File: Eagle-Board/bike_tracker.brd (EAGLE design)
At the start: 100 x 80 mm, 16 parts, among them J1 TRANSFLASH-LOCK

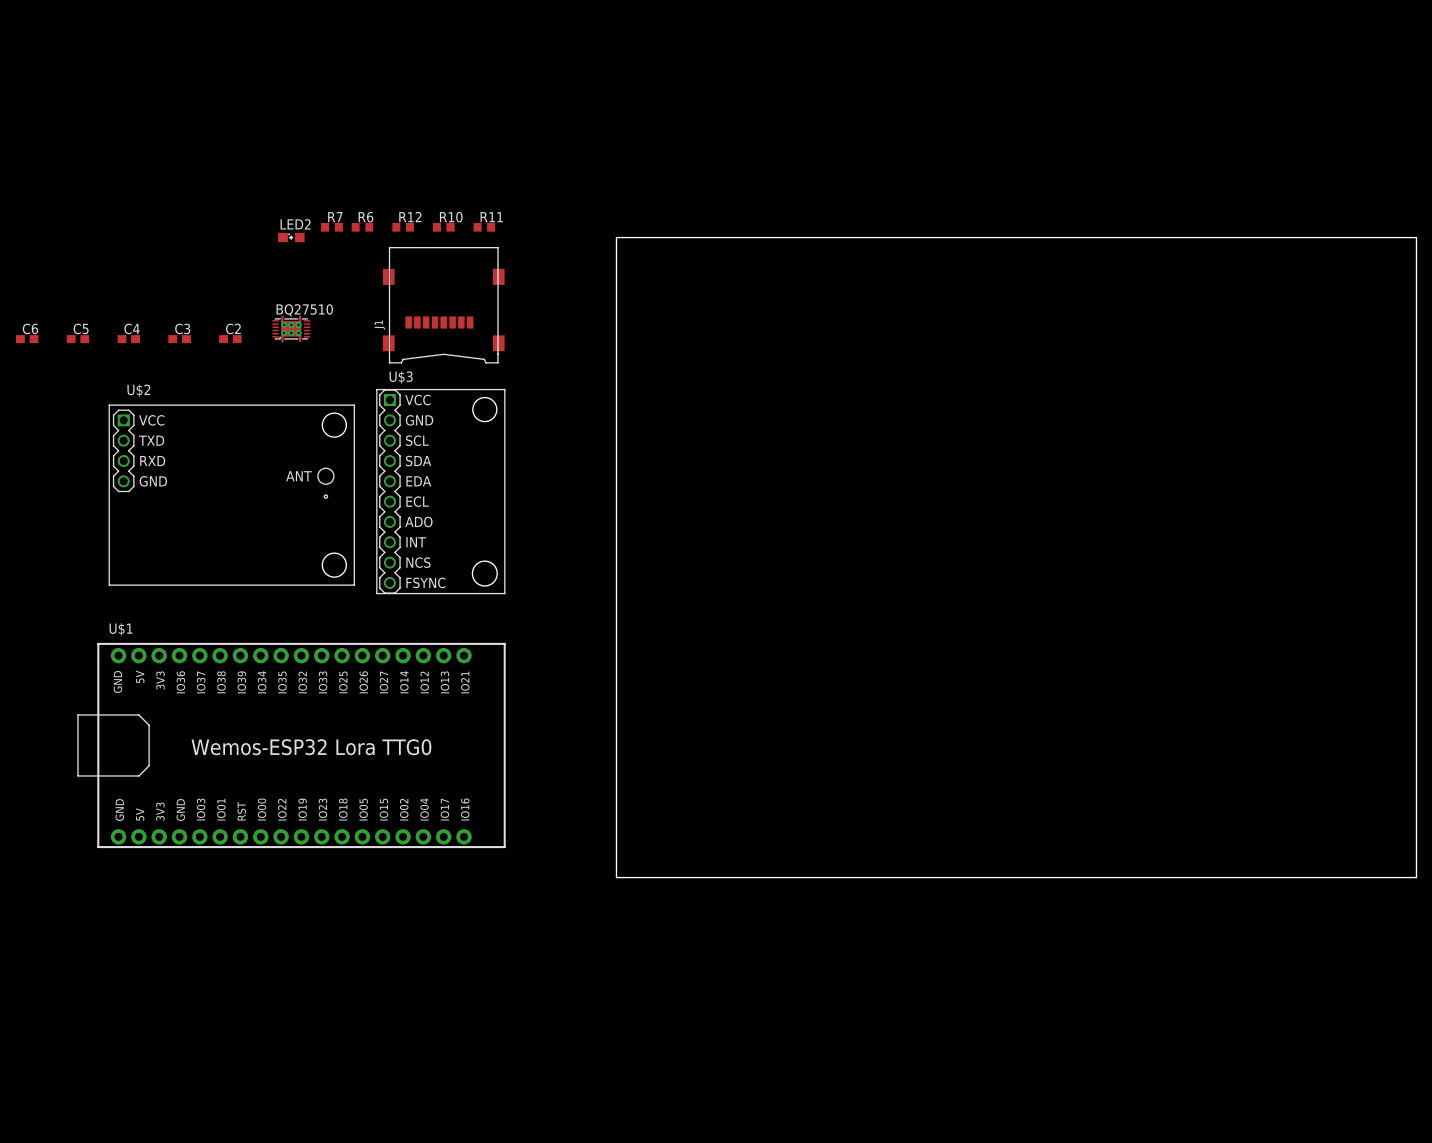
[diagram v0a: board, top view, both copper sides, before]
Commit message: board design ready - revising and exporting for gerber - SeeedStudio Fusion files added
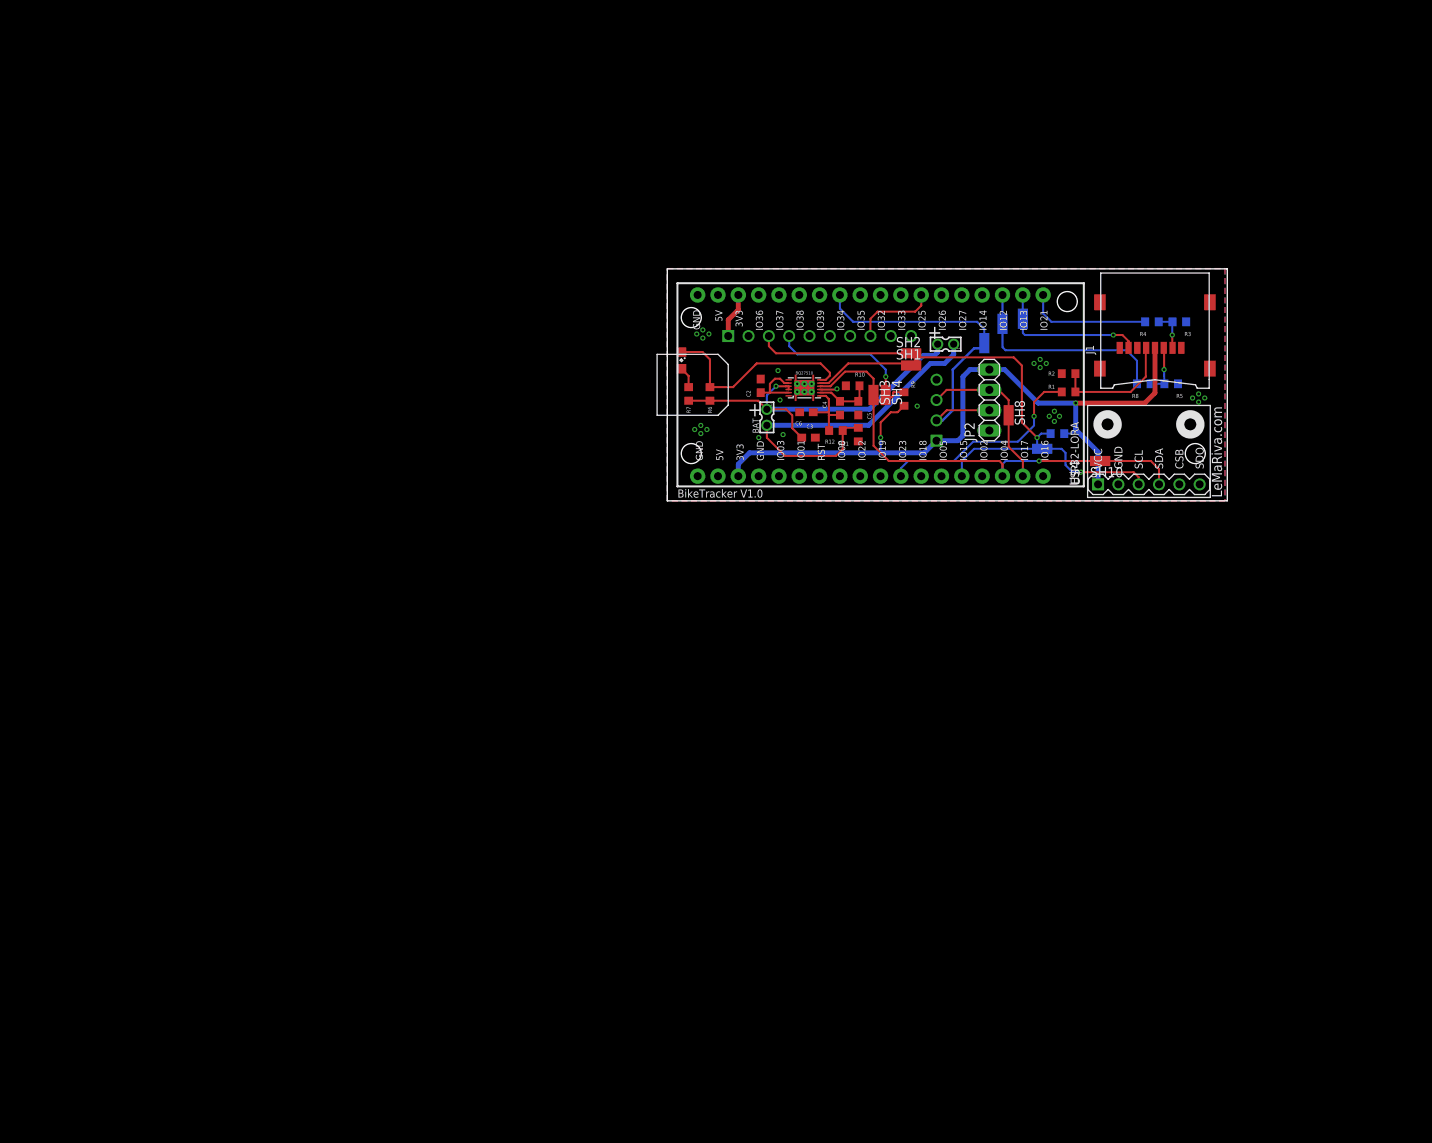
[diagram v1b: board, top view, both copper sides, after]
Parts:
- removed LED2: (no value), led:SML0805
- removed U$1: ESP32LORA, ESP32-DEVKITC:ESP32-LORA-TTGO
- added BAT, BAT-IN: 332-02, con-garry:332-02
- added ESP32-LORA: ESP32LORA, ESP32-DEVKITC:ESP32-LORA-TTGO
- added JP2: (no value), pinhead:1X04
- added LOW-BAT: (no value), led:SML0805
- added R1, R4, R8: 4k7, resistor:R0603
- added R13, R2, R3, R5, R9: 10k, resistor:R0603
- added SH1, SH10, SH2, SH3, SH4, SH5, SH6, SH7, SH8, SH9: SHORTT5, shorts:SHORT_TOP-50
- added U$4: BME280, diy-modules:BME280
- C4, C5, C6: value 0.47u -> 0.1u
- U$3: value IMU9255 -> MPU9255
- moved U$2 103.1 mm to (54.6, 64.8), flipped to the bottom, turned to 180 degrees
- moved C5 97.9 mm to (30.2, 58.7), turned to 270 degrees
- moved C6 97.8 mm to (23.7, 58.2)
- moved C4 89.3 mm to (27.9, 58.7), turned to 270 degrees
- moved J1 89.0 mm to (67.3, 66.7)
- moved C3 79.6 mm to (24.0, 55.0)
- moved C2 66.6 mm to (18.0, 61.5), turned to 90 degrees
- moved BQ27510 64.6 mm to (23.5, 61.2)
- moved R12 59.8 mm to (27.4, 55.9)
- moved R10 54.8 mm to (29.5, 61.5)
- moved R11 53.4 mm to (30.2, 55.4), turned to 90 degrees
- moved R7 49.2 mm to (9.02, 60.5), turned to 270 degrees
- moved R6 48.2 mm to (11.7, 60.5), turned to 270 degrees
- moved U$3 45.6 mm to (24.1, 59.7), flipped to the bottom, turned to 270 degrees
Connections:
- removed net RXD: U$2.3
- removed net VCC: U$3.1
- new net INT-IMU: ESP32-LORA.25, U$3.8
- new net MISO-SD: J1.7, SH6.1
- new net MOSI-SD: R8.2, SH5.1
- new net N$1: J1.5, R1.1, R2.2
- new net N$2: J1.2, R3.2, R4.1
- new net N$3: J1.3, R5.2, R8.1
- new net RX: ESP32-LORA.29, SH7.2
- new net RXD_NEO: JP2.3, SH8.1, U$2.3
- new net SCL: ESP32-LORA.14, R13.2, SH1.2, SH2.2, SH9.2
- new net SCL-BME: SH9.1, U$4.3
- new net SCL-IMU: SH2.1, U$3.3
- new net SDA: ESP32-LORA.16, R9.2, SH10.2, SH3.2, SH4.2
- new net SDA-BME: SH10.1, U$4.4
- new net SDA-IMU: SH4.1, U$3.4
- new net SPI-CLK: ESP32-LORA.11, R1.2
- new net SPI-CS: ESP32-LORA.19, R4.2
- new net SPI-MISO: ESP32-LORA.21, SH5.2
- new net SPI-MOSI: ESP32-LORA.20, SH6.2
- new net TX: ESP32-LORA.17, SH8.2
- new net TXD-NEO: JP2.2, SH7.1, U$2.2
- net !BAT_LOW: now also LOW-BAT.C; no longer LED2.C
- net 5V: now also ESP32-LORA.2, ESP32-LORA.35; no longer U$1.2, U$1.35
- net GND: now also ESP32-LORA.1, ESP32-LORA.36, ESP32-LORA.4, JP2.1, R2.1, R3.1, R5.1, U$2.4, U$4.2; no longer U$1.1, U$1.36, U$1.4
- net N$9: now also LOW-BAT.A; no longer LED2.A
- net SCL_BQ27510: now also SH1.1
- net SDA_BQ27510: now also SH3.1
- net VBAT+: now also BAT-IN.2, BAT.1
- net VBAT-: now also BAT-IN.1, BAT.2
- net VDD: now also ESP32-LORA.3, ESP32-LORA.34, JP2.4, R13.1, R9.1, U$2.1, U$3.1, U$4.1
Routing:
- net VDD: track 0.00 -> 97.0 mm, vias 0 -> 2
- net VBAT+: track 0.00 -> 47.7 mm, vias 0 -> 1
- net VBAT-: track 0.00 -> 45.1 mm
- net SDA: track 0.00 -> 42.0 mm, vias 0 -> 1
- net SCL: track 0.00 -> 40.5 mm, vias 0 -> 1
- net SPI-CLK: track 0.00 -> 26.8 mm, vias 0 -> 1
- net !BAT_LOW: track 0.00 -> 25.9 mm
- net MOSI-SD: track 0.00 -> 22.7 mm
- net RX: track 0.00 -> 21.9 mm
- net TXD-NEO: track 0.00 -> 19.8 mm
- net SCL-IMU: track 0.00 -> 18.8 mm
- net SDA-IMU: track 0.00 -> 17.1 mm, vias 0 -> 1
- net MISO-SD: track 0.00 -> 15.6 mm, vias 0 -> 1
- net SPI-CS: track 0.00 -> 15.5 mm
- net N$1: track 0.00 -> 15.5 mm
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- added copper zone on layer 1, net GND
- added copper zone on layer 16, net GND
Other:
- board size 100 x 80 mm -> 70 x 29 mm
- board text added: "+"
- board text added: "BikeTracker V1.0"
- board text added: "LeMaRiva.com"

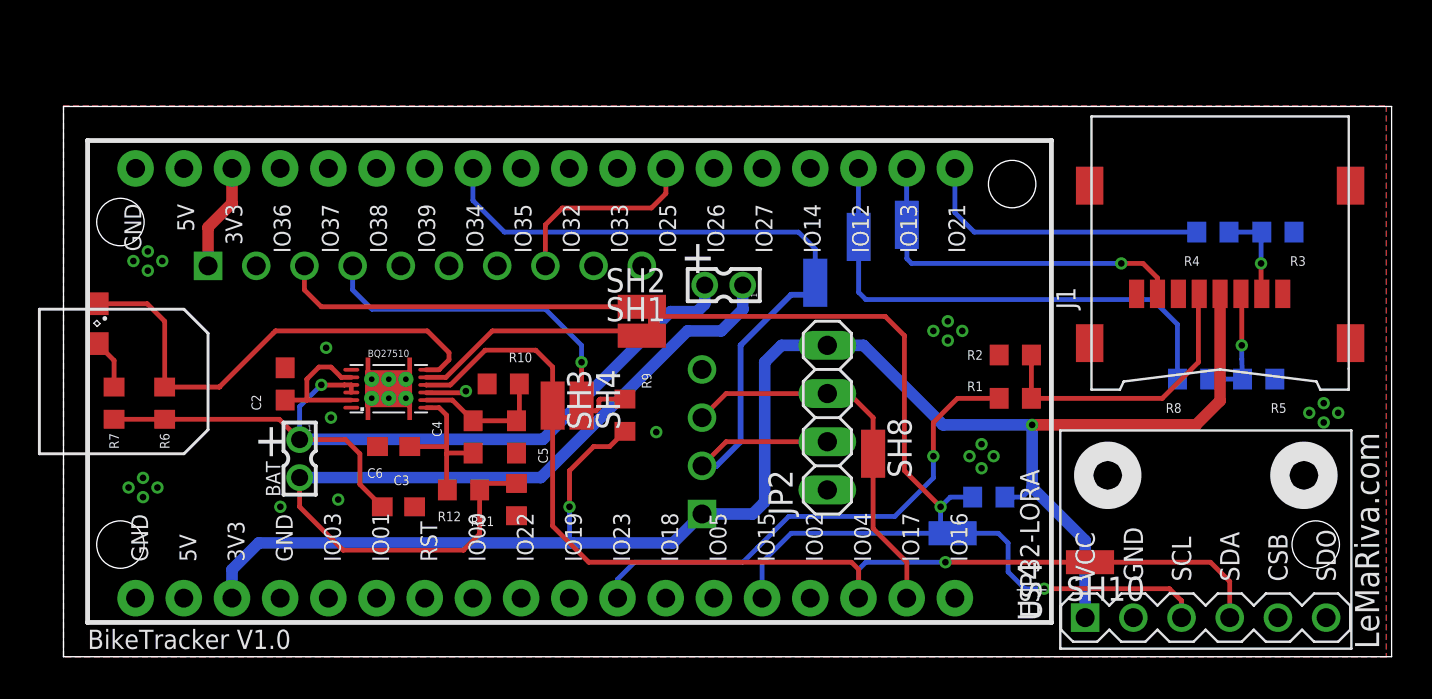
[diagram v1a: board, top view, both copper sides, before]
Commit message: texas and switch libraries added final version with buttons and possibility to switch off/on external devices
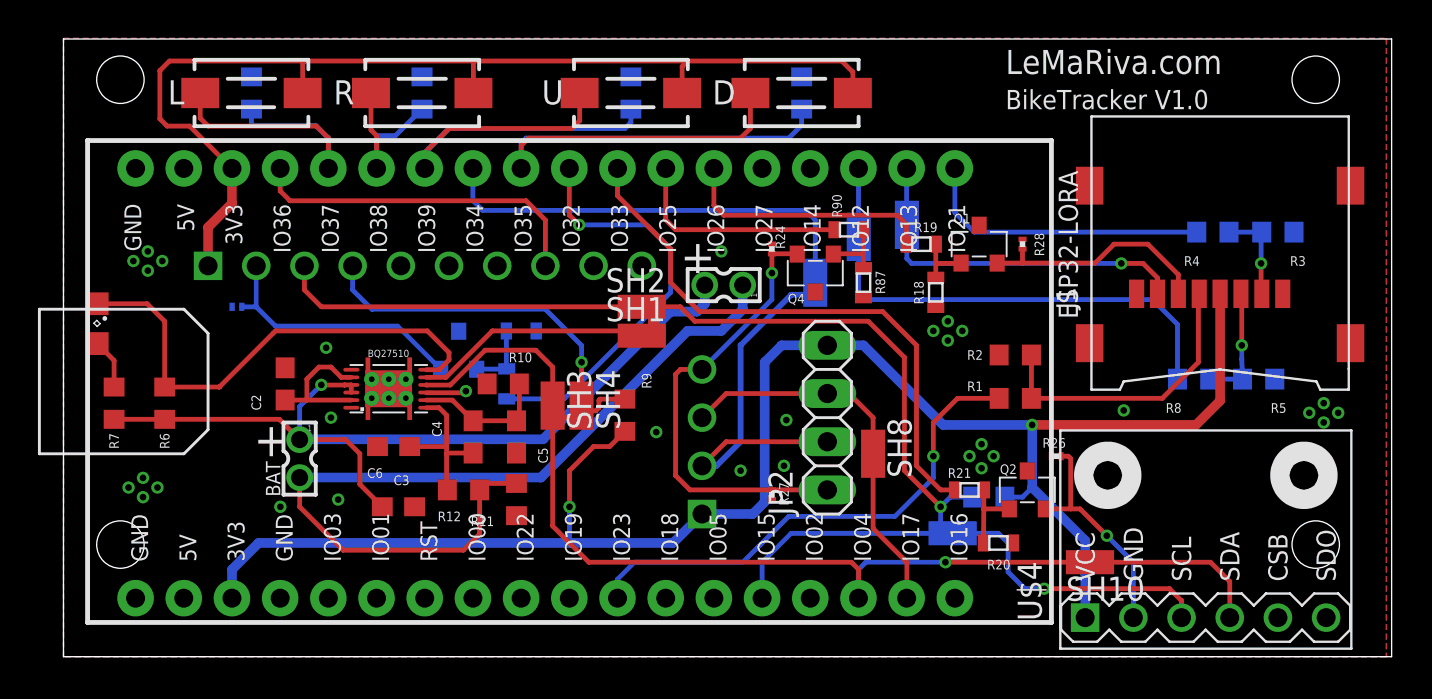
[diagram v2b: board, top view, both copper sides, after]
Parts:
- added D, L, R, U: DTSM-3, switch-tact:DTSM-3
- added Q1, Q2, Q3, Q4: IRLML5203, transistor-power:MICRO3
- added R14, R15, R16, R17: 10k, resistor:R0603
- added R18, R20, R22, R87: 10k, ssmd:0603
- added R19, R21, R23, R90: 470R, ssmd:0603
- added R24, R25, R26, R27, R28: (no value), resistor:R0201
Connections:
- new net GND_BME: Q2.2, R26.2, U$4.2
- new net GND_GPS: JP2.1, Q4.2, R24.2, R27.2, U$2.4
- new net GND_MPU: Q3.2, R25.2, U$3.2
- new net GND_SD: J1.6, Q1.2, R28.1
- new net IO25: ESP32-LORA.25, R90.2
- new net IO26: ESP32-LORA.24, R19.2
- new net IO32: ESP32-LORA.27, R23.2
- new net IO33: ESP32-LORA.26, R21.2
- new net IO35: D.1, ESP32-LORA.28, R17.2
- new net IO37: ESP32-LORA.32, L.1, R15.2
- new net IO38: ESP32-LORA.31, R.1, R16.2
- new net IO39: ESP32-LORA.30, R14.2, U.1
- new net N$12: ESP32-LORA.13
- new net N$4: Q4.1, R87.2, R90.1
- new net N$5: Q1.1, R18.2, R19.1
- new net N$6: Q2.1, R20.2, R21.1
- new net N$8: Q3.1, R22.2, R23.1
- net GND: now also Q1.3, Q2.3, Q3.3, Q4.3, R14.1, R15.1, R16.1, R17.1, R18.1, R20.1, R22.1, R24.1, R25.1, R26.1, R27.1, R28.2, R87.1; no longer J1.6, JP2.1, U$2.4, U$3.2, U$4.2
- net INT-IMU: now also ESP32-LORA.33; no longer ESP32-LORA.25
- net VDD: now also D.2, L.2, R.2, U.2
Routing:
- net VDD: track 97.0 -> 147.7 mm
- net IO35: track 0.00 -> 32.9 mm
- net IO33: track 0.00 -> 30.4 mm
- net IO39: track 0.00 -> 24.2 mm
- net GND_GPS: track 0.00 -> 24.1 mm, vias 0 -> 1
- net IO32: track 0.00 -> 21.8 mm, vias 0 -> 1
- net IO37: track 0.00 -> 16.8 mm
- net GND_MPU: track 0.00 -> 14.0 mm
- net IO26: track 0.00 -> 13.6 mm
- net GND_SD: track 0.00 -> 12.4 mm
- net GND_BME: track 0.00 -> 11.9 mm, vias 0 -> 1
- net IO25: track 0.00 -> 11.8 mm
- net IO38: track 0.00 -> 8.80 mm
- net INT-IMU: track 10.5 -> 18.2 mm
- net PWPD: track 0.00 -> 5.43 mm
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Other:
- board size 70 x 29 mm -> 70 x 32.6 mm

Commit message: minor modifications made
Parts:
- moved Q1 2.01 mm to (55.8, 67.2)
- moved R28 1.63 mm to (57.9, 67.6), turned to 180 degrees
- moved R26 1.28 mm to (57.4, 57.8)
- moved U$2 0.63 mm to (55.2, 64.8)
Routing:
- net TXD-NEO: track 19.8 -> 17.7 mm
- net N$5: track 3.11 -> 4.94 mm
- net GND_BME: track 11.9 -> 13.3 mm
- net GND_SD: track 12.4 -> 13.3 mm
- net RXD_NEO: track 11.3 -> 10.7 mm
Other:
- board size 70 x 32.6 mm -> 70 x 33 mm

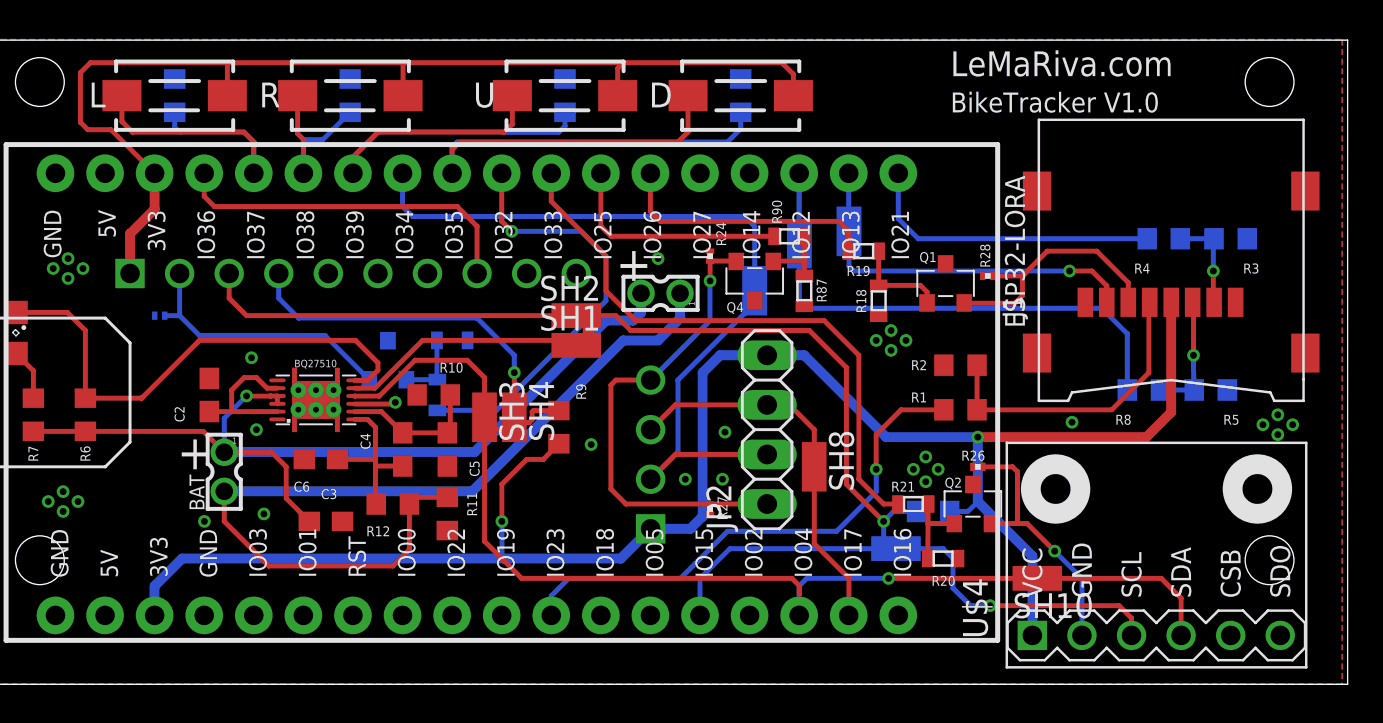
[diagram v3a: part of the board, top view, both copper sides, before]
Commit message: updated rev1.1 -> added RTC chip (DS1339)
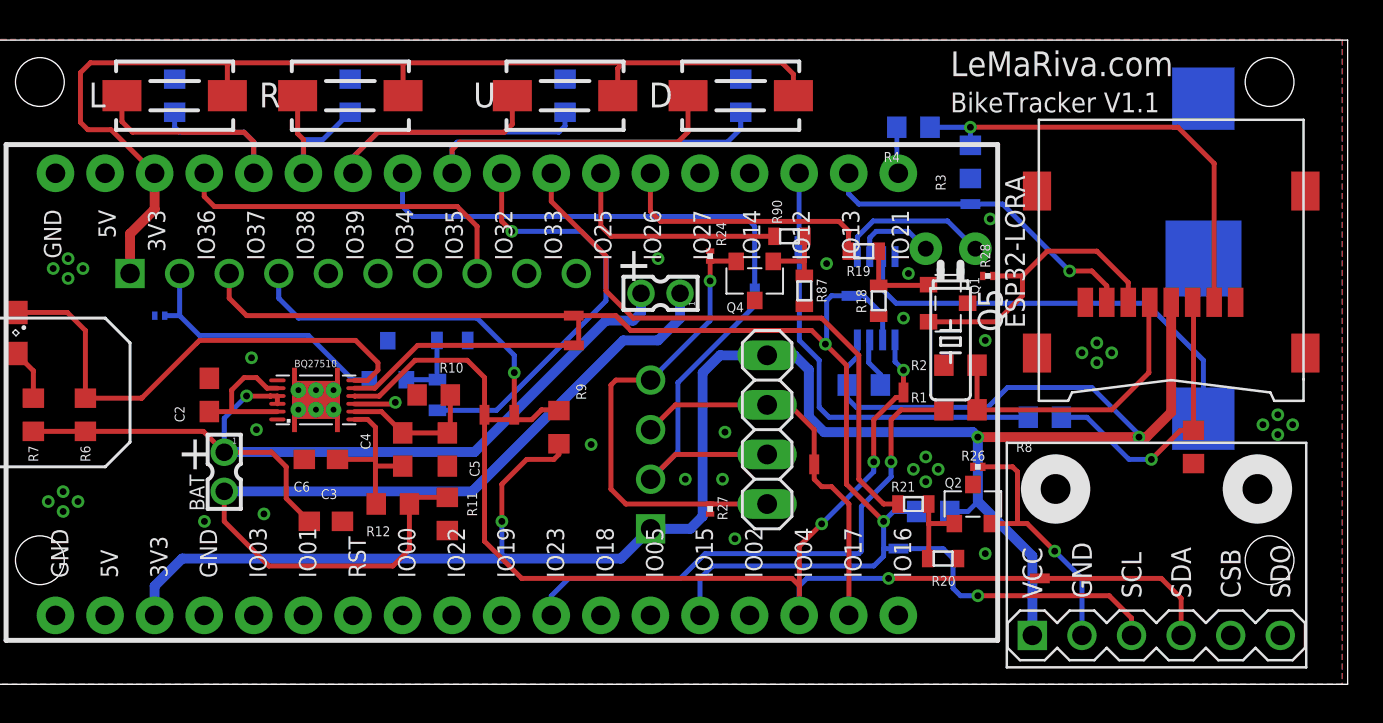
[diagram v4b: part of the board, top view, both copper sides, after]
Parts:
- added Q5: (no value), adafruit:TC26H
- added R29: (no value), resistor:R0603
- added SH11, SH12: SHORT, shorts:SHORT_TOP-20
- added U$1: DS1339, adafruit:SOPM08
- added U$5: (no value), adafruit:CR1220-SMD
- SH1, SH10, SH2, SH3, SH4, SH5, SH6, SH7, SH8, SH9: value SHORTT5 -> SHORT; device shorts:SHORT_TOP-50 -> shorts:SHORT_TOP-20
- moved R4 14.0 mm to (54.1, 75.2)
- moved R3 13.9 mm to (57.0, 73.4), turned to 90 degrees
- moved SH6 6.25 mm to (56.9, 71.2), turned to 180 degrees
- moved R8 5.27 mm to (60.8, 60.3)
- moved R5 3.05 mm to (68.5, 58.8), flipped to the top, turned to 90 degrees
- moved Q1 1.02 mm to (55.9, 66.2), turned to 270 degrees
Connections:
- new net INT-CLK: R29.2, U$1.7
- new net N$10: Q5.1, U$1.1
- new net N$13: Q5.2, U$1.2
- new net N$15: U$1.3, U$5.+$1
- new net SCL-CLK: SH12.1, U$1.6
- new net SDA-CLK: SH11.1, U$1.5
- net GND: now also U$1.4, U$5.-
- net SCL: now also SH12.2
- net SDA: now also SH11.2
- net VDD: now also R29.1, U$1.8
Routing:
- net N$15: track 0.00 -> 23.7 mm
- net VDD: track 147.7 -> 169.5 mm, vias 2 -> 3
- net N$2: track 5.02 -> 23.4 mm
- net SPI-CS: track 15.5 -> 2.39 mm
- net SDA: track 42.0 -> 54.7 mm, vias 1 -> 3
- net N$3: track 6.24 -> 14.9 mm
- net N$10: track 0.00 -> 7.99 mm
- net MISO-SD: track 15.6 -> 9.31 mm
- net SPI-MOSI: track 2.34 -> 7.25 mm
- net N$13: track 0.00 -> 4.34 mm
- net SCL: track 40.1 -> 44.4 mm, vias 1 -> 2
- net MOSI-SD: track 22.7 -> 19.3 mm
- net SCL-CLK: track 0.00 -> 3.04 mm
- net SDA-CLK: track 0.00 -> 2.62 mm, vias 0 -> 1
- net INT-CLK: track 0.00 -> 2.58 mm
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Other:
- board text added: "BikeTracker V1.1"
- board text removed: "BikeTracker V1.0"
